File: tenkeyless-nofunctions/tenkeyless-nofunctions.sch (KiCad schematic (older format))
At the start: 142 parts, among them SW1 TILDE, SW10 NUM_9, SW11 NUM_0, SW12 UNDRSCR, SW13 EQUAL, SW14 BCKSPC, SW15 INSRT, SW16 HOME, SW17 PG_UP, SW18 LTAB, SW19 KEY_Q, SW2 NUM_1, SW20 KEY_W, SW21 KEY_E, SW22 KEY_R, SW23 KEY_T, SW24 KEY_Y, SW25 KEY_U, SW26 KEY_I, SW27 KEY_O, SW28 KEY_P, SW29 OP_BRKT, SW3 NUM_2, SW30 CL_BRKT, SW31 BKSLSH, SW32 DELETE, SW33 END, SW34 PG_DN, SW35 CAPS, SW36 KEY_A, SW37 KEY_S, SW38 KEY_D, SW39 KEY_F, SW4 NUM_3, SW40 KEY_G, SW41 KEY_H, SW42 KEY_J, SW43 KEY_K, SW44 KEY_L, SW45 SEMICOLON, SW46 QUOTE, SW47 ENTER, SW48 LSHIFT, SW49 KEY_Z, SW5 NUM_4, SW50 KEY_X, SW51 KEY_C, SW52 KEY_V, SW53 KEY_B, SW54 KEY_N, SW55 KEY_M, SW56 COMMA, SW57 PERIOD, SW58 FWDSLSH, SW59 RSHIFT, SW6 NUM_5, SW60 UP, SW61 LCTRL, SW62 WIN, SW63 LALT, SW64 SPACE, SW65 RALT, SW66 RCTRL, SW67 FN, SW68 ESC, SW69 LEFT, SW7 NUM_6, SW70 DN, SW71 RIGHT, SW8 NUM_7, SW9 NUM_8

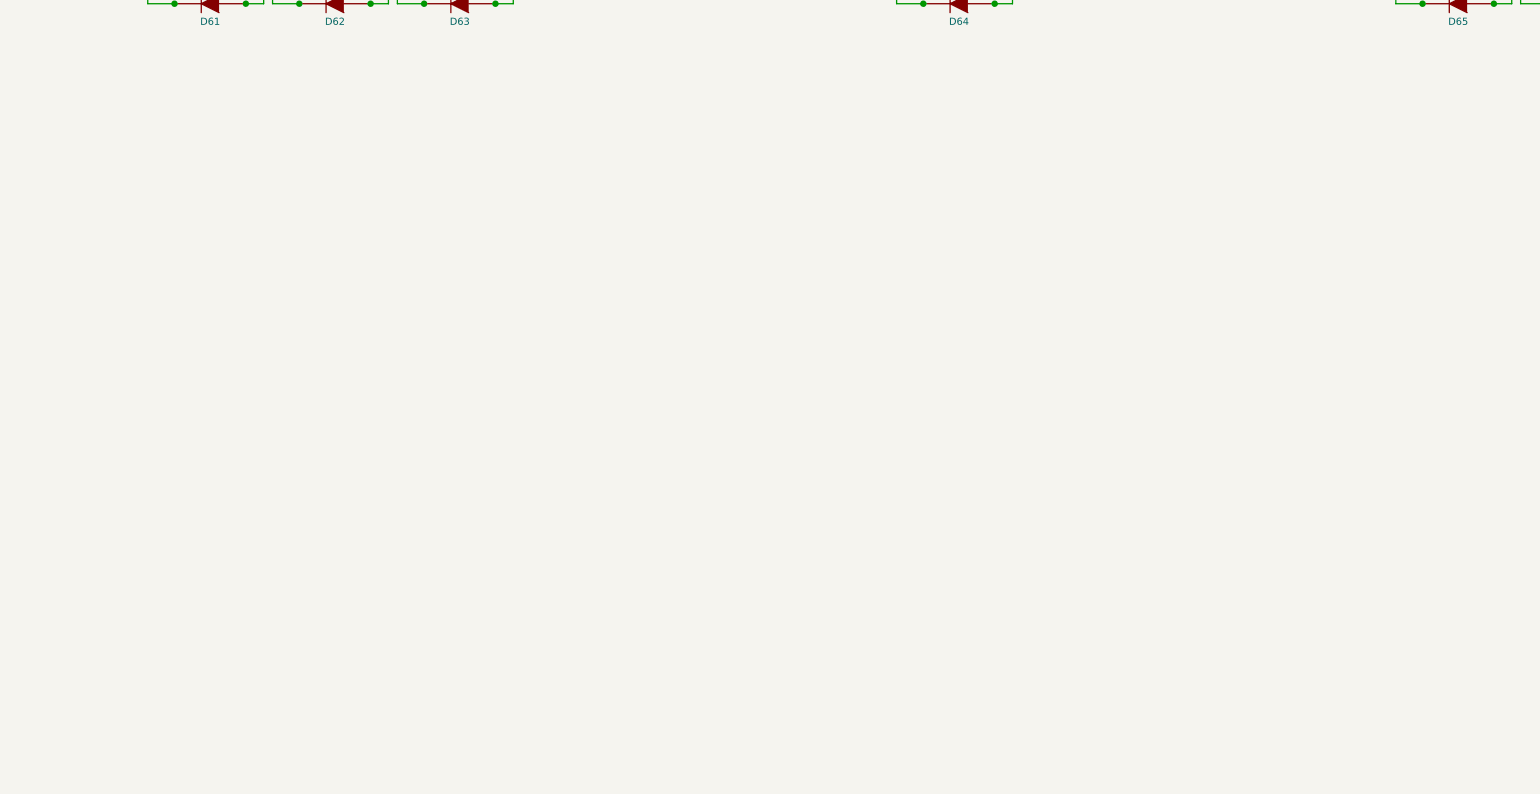
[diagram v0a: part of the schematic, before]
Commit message: we're going to have to switch to the Teensie2.0++
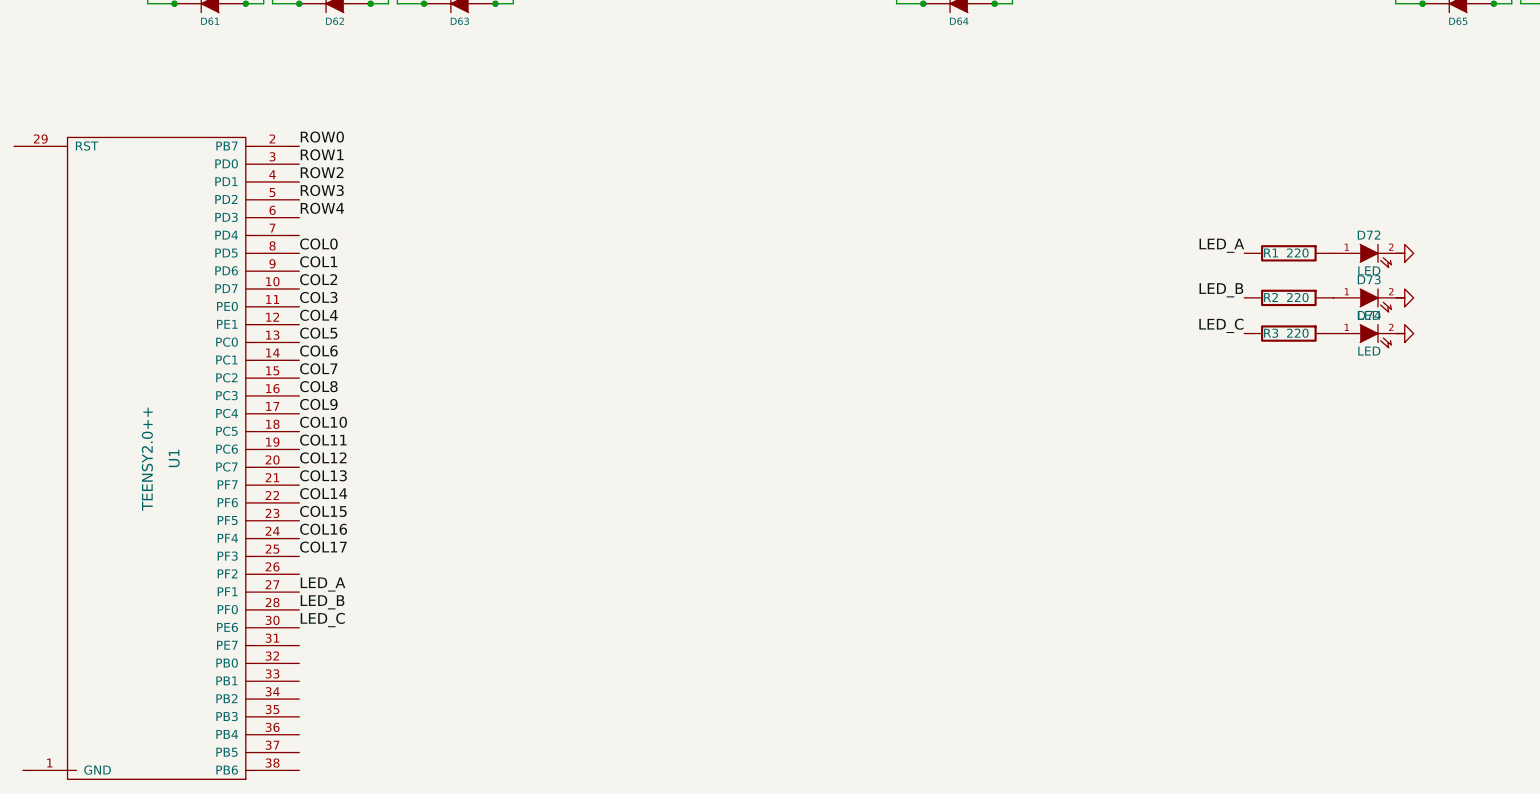
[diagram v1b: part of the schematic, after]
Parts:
- added D72, D73, D74: LED, symbol LED
- added R1, R2, R3: 220, symbol RESISTOR
- added U1: TEENSY2.0++, symbol TEENSY2.0++
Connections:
- net COL0: now also U1.8 (PD5)
- net COL1: now also U1.9 (PD6)
- net COL10: now also U1.18 (PC5)
- net COL11: now also U1.19 (PC6)
- net COL12: now also U1.20 (PC7)
- net COL13: now also U1.21 (PF7)
- net COL14: now also U1.22 (PF6)
- net COL15: now also U1.23 (PF5)
- net COL16: now also U1.24 (PF4)
- net COL17: now also U1.25 (PF3)
- net COL2: now also U1.10 (PD7)
- net COL3: now also U1.11 (PE0)
- net COL4: now also U1.12 (PE1)
- net COL5: now also U1.13 (PC0)
- net COL6: now also U1.14 (PC1)
- net COL7: now also U1.15 (PC2)
- net COL9: now also U1.17 (PC4)
- net ROW0: now also U1.2 (PB7)
- net ROW1: now also U1.3 (PD0)
- net ROW2: now also U1.4 (PD1)
- net ROW3: now also U1.5 (PD2)
- net ROW4: now also U1.6 (PD3)
- new net: D72.1 (A), R1.1
- new net: D73.1 (A), R2.1
- new net: D74.1 (A), R3.1
- new net COL8: U1.16 (PC3)
- new net LED_A: R1.2, U1.27 (PF1)
- new net LED_B: R2.2, U1.28 (PF0)
- new net LED_C: R3.2, U1.30 (PE6)
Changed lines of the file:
@@
 EESchema Schematic File Version 2
+LIBS:Keyboard
 LIBS:power
 LIBS:device
@@
 Text Label 13100 1100 1    60   ~ 0
 COL17
+$Comp
+L TEENSY2.0++ U1
+U 1 1 56FEC65F
+P 2000 8450
+F 0 "U1" V 2050 8450 60  0000 C CNN
+F 1 "TEENSY2.0++" V 1900 8450 60  0000 C CNN
+F 2 "" H 1950 9250 60  0000 C CNN
+F 3 "" H 1950 9250 60  0000 C CNN
+	1    2000 8450
+	1    0    0    -1
+$EndComp
+$Comp
+L RESISTOR R1
+U 1 1 56FEC673
+P 8300 7300
+F 0 "R1" V 8300 7200 50  0000 C CNN
+F 1 "220" V 8300 7350 50  0000 C CNN
+F 2 "" H 8300 7300 60  0000 C CNN
+F 3 "" H 8300 7300 60  0000 C CNN
+	1    8300 7300
+	0    1    1    0
+$EndComp
+$Comp
+L LED D72
+U 1 1 56FEC687
+P 8750 7300
+F 0 "D72" H 8750 7400 50  0000 C CNN
+F 1 "LED" H 8750 7200 50  0000 C CNN
+F 2 "" H 8750 7300 60  0000 C CNN
+F 3 "" H 8750 7300 60  0000 C CNN
+	1    8750 7300
+	1    0    0    -1
+$EndComp
+$Comp
+L GND #PWR1
+U 1 1 56FEC69B
+P 8950 7300
+F 0 "#PWR1" H 8950 7300 30  0001 C CNN
+F 1 "GND" H 8950 7230 30  0001 C CNN
+F 2 "" H 8950 7300 60  0000 C CNN
+F 3 "" H 8950 7300 60  0000 C CNN
+	1    8950 7300
+	0    -1   -1   0
+$EndComp
+Text Label 8050 7300 2    60   ~ 0
+LED_A
+$Comp
+L RESISTOR R2
+U 1 1 56FEC6BD
+P 8300 7550
+F 0 "R2" V 8300 7450 50  0000 C CNN
+F 1 "220" V 8300 7600 50  0000 C CNN
+F 2 "" H 8300 7550 60  0000 C CNN
+F 3 "" H 8300 7550 60  0000 C CNN
+	1    8300 7550
+	0    1    1    0
+$EndComp
+$Comp
+L LED D73
+U 1 1 56FEC6C3
+P 8750 7550
+F 0 "D73" H 8750 7650 50  0000 C CNN
+F 1 "LED" H 8750 7450 50  0000 C CNN
+F 2 "" H 8750 7550 60  0000 C CNN
+F 3 "" H 8750 7550 60  0000 C CNN
+	1    8750 7550
+	1    0    0    -1
+$EndComp
+$Comp
+L GND #PWR2
+U 1 1 56FEC6C9
+P 8950 7550
+F 0 "#PWR2" H 8950 7550 30  0001 C CNN
+F 1 "GND" H 8950 7480 30  0001 C CNN
+F 2 "" H 8950 7550 60  0000 C CNN
+F 3 "" H 8950 7550 60  0000 C CNN
+	1    8950 7550
+	0    -1   -1   0
+$EndComp
+Text Label 8050 7550 2    60   ~ 0
+LED_B
+$Comp
+L RESISTOR R3
+U 1 1 56FEC6D0
+P 8300 7750
+F 0 "R3" V 8300 7650 50  0000 C CNN
+F 1 "220" V 8300 7800 50  0000 C CNN
+F 2 "" H 8300 7750 60  0000 C CNN
+F 3 "" H 8300 7750 60  0000 C CNN
+	1    8300 7750
+	0    1    1    0
+$EndComp
+$Comp
+L LED D74
+U 1 1 56FEC6D6
+P 8750 7750
+F 0 "D74" H 8750 7850 50  0000 C CNN
+F 1 "LED" H 8750 7650 50  0000 C CNN
+F 2 "" H 8750 7750 60  0000 C CNN
+F 3 "" H 8750 7750 60  0000 C CNN
+	1    8750 7750
+	1    0    0    -1
+$EndComp
+$Comp
+L GND #PWR3
+U 1 1 56FEC6DC
+P 8950 7750
+F 0 "#PWR3" H 8950 7750 30  0001 C CNN
+F 1 "GND" H 8950 7680 30  0001 C CNN
+F 2 "" H 8950 7750 60  0000 C CNN
+F 3 "" H 8950 7750 60  0000 C CNN
+	1    8950 7750
+	0    -1   -1   0
+$EndComp
+Text Label 8050 7750 2    60   ~ 0
+LED_C
+Text Label 2750 6700 0    60   ~ 0
+ROW0
+Text Label 2750 6800 0    60   ~ 0
+ROW1
+Text Label 2750 6900 0    60   ~ 0
+ROW2
+Text Label 2750 7000 0    60   ~ 0
+ROW3
+Text Label 2750 7100 0    60   ~ 0
+ROW4
+Text Label 2750 7300 0    60   ~ 0
+COL0
+Text Label 2750 7400 0    60   ~ 0
+COL1
+Text Label 2750 7500 0    60   ~ 0
+COL2
+Text Label 2750 7600 0    60   ~ 0
+COL3
+Text Label 2750 7700 0    60   ~ 0
+COL4
+Text Label 2750 7800 0    60   ~ 0
+COL5
+Text Label 2750 7900 0    60   ~ 0
+COL6
+Text Label 2750 8000 0    60   ~ 0
+COL7
+Text Label 2750 8100 0    60   ~ 0
+COL8
+Text Label 2750 8200 0    60   ~ 0
+COL9
+Text Label 2750 8300 0    60   ~ 0
+COL10
+Text Label 2750 8400 0    60   ~ 0
+COL11
+Text Label 2750 8500 0    60   ~ 0
+COL12
+Text Label 2750 8600 0    60   ~ 0
+COL13
+Text Label 2750 8700 0    60   ~ 0
+COL14
+Text Label 2750 8800 0    60   ~ 0
+COL15
+Text Label 2750 8900 0    60   ~ 0
+COL16
+Text Label 2750 9000 0    60   ~ 0
+COL17
+Text Label 2750 9200 0    60   ~ 0
+LED_A
+Text Label 2750 9300 0    60   ~ 0
+LED_B
+Text Label 2750 9400 0    60   ~ 0
+LED_C
 $EndSCHEMATC
